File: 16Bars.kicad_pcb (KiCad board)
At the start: 2 copper layers, 28.5 x 105 mm, 40 parts, among them IC1 CD4033BE, IC2 CD4033BE, IC3 CD4510BE, J1 3.5mm_Mono_Switched, J2 Conn_02x05_Odd_Even, Q1 2N3904, Q2 2N3904, Q3 2N3904, Q4 2N3904, Q5 NPN BJT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

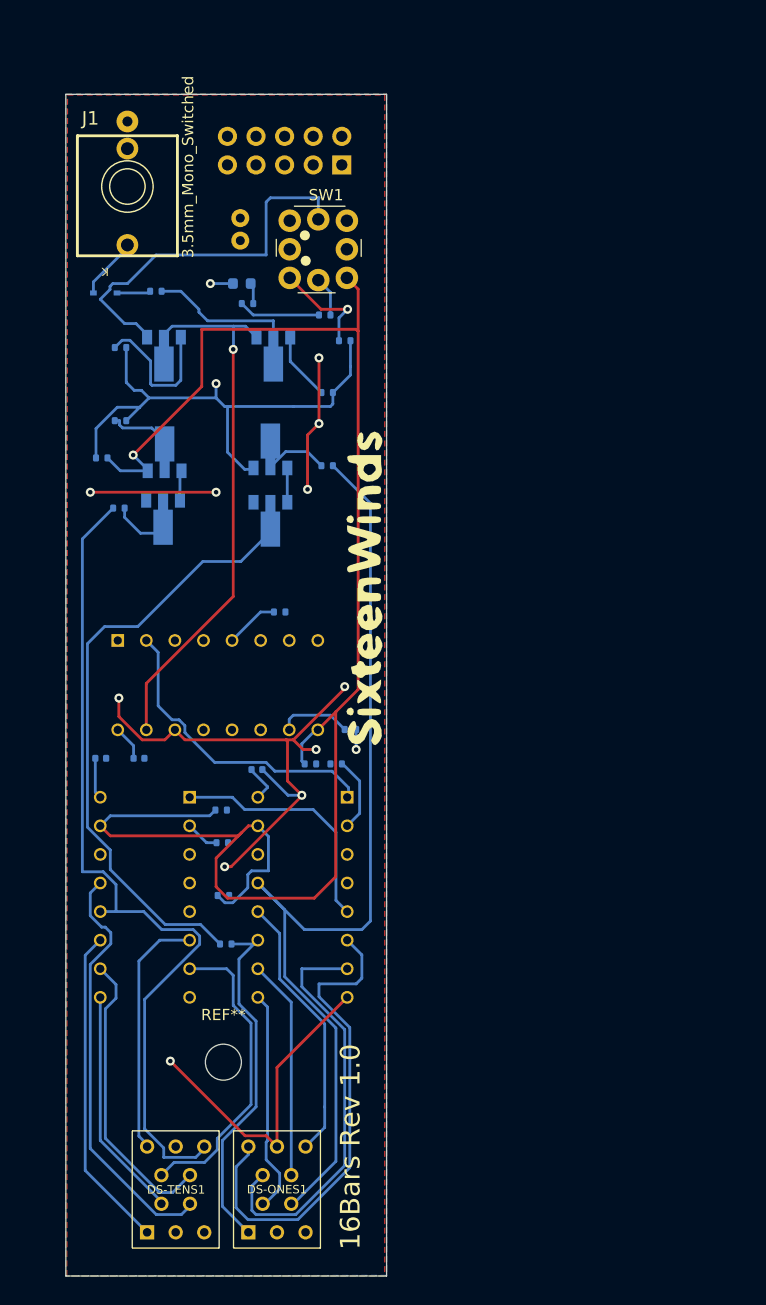
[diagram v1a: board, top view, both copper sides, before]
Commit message: Update PCB with V2 changes
F.Cu SMD assembly will provide much more room for tracks instead of routing around ICs on B.Cu.
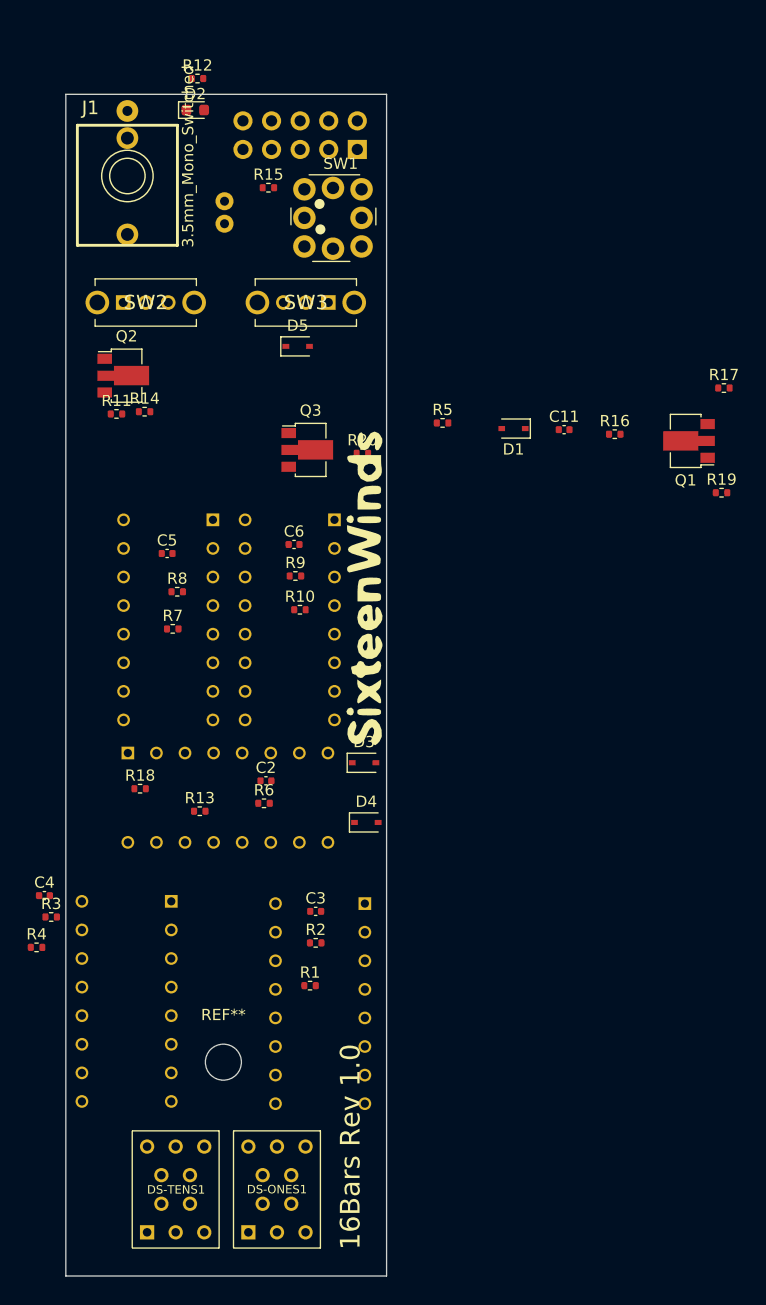
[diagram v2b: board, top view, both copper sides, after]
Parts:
- removed Q4, Q6: 2N3904, Package_TO_SOT_SMD:SOT-89-3
- removed Q5: NPN BJT, Package_TO_SOT_SMD:SOT-89-3
- added C11: 330pf, Capacitor_SMD:C_0402_1005Metric, F.Cu at (100.8, 64.8)
- added C5: 100nf, Capacitor_SMD:C_0402_1005Metric, F.Cu at (65.5, 75.8)
- added C6: 100nf, Capacitor_SMD:C_0402_1005Metric, F.Cu at (76.8, 75.0)
- added D3: 1N5819WS, Diode_SMD:D_SOD-323, F.Cu at (83.0, 94.4)
- added D4: 1N5819WS, Diode_SMD:D_SOD-323, F.Cu at (83.2, 99.7)
- added D5: 1N5819WS, Diode_SMD:D_SOD-323, F.Cu at (77.1, 57.4)
- added IC4: CD4510BE, SamacSys_Parts:DIP794W53P254L1930H508Q16N, B.Cu at (65.6, 81.7)
- added IC5: CD4510BE, SamacSys_Parts:DIP794W53P254L1930H508Q16N, B.Cu at (76.4, 81.7)
- added R19: 10K, Resistor_SMD:R_0402_1005Metric, F.Cu at (114.8, 70.4)
- added R20: 10K, Resistor_SMD:R_0402_1005Metric, F.Cu at (82.9, 66.9)
- added SW2: SW_SPDT - EG1249, EG1249:EG1249, F.Cu at (61.6, 53.5)
- added SW3: SW_SPDT-EG1249, EG1249:EG1249, F.Cu at (79.8, 53.5)
- C2, C3, C4, D2, Q1, Q2, Q3, R1, R10, R11, R12, R13, R14, R15, R16, R17, R18, R2, R3, R4, R6, R7, R8, R9: moved to F.Cu
- D1: value 1N4148 -> 1N5819WS; moved to F.Cu
- R5: value 47K -> 470; moved to F.Cu
- moved R17 55.6 mm to (115.0, 61.1), turned to 0 degrees
- moved R11 48.1 mm to (61.0, 63.4), turned to 0 degrees
- moved D1 38.2 mm to (96.3, 64.7)
- moved Q1 37.7 mm to (111.9, 65.8), turned to 180 degrees
- moved R13 35.4 mm to (68.4, 98.7), turned to 0 degrees
- moved R5 28.0 mm to (90.0, 64.2), turned to 0 degrees
- moved R7 25.4 mm to (66.0, 82.5), turned to 0 degrees
- moved R16 25.4 mm to (105.3, 65.2), turned to 0 degrees
- moved C3 23.4 mm to (78.7, 107.6), turned to 0 degrees
- moved R8 22.2 mm to (66.4, 79.2), turned to 0 degrees
- moved C4 22.0 mm to (54.6, 106.2), turned to 0 degrees
- moved R12 20.5 mm to (68.2, 33.6)
- moved R4 20.4 mm to (53.9, 110.8), turned to 0 degrees
- moved R1 19.8 mm to (78.2, 114.2), turned to 0 degrees
- moved R18 19.4 mm to (63.1, 96.7), turned to 0 degrees
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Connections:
- C2 pad 1: +12V -> GND
- C2 pad 2: GND -> +12V
- D1 pad 1: Net-(D1-Pad1) -> Net-(C11-Pad1)
- D1 pad 2: Net-(D1-Pad2) -> Net-(R5-Pad1)
- IC1 pad 15: /16_BARS_RESET -> /RESET
- IC2 pad 14: unconnected-(IC2-Pad14) -> GND
- IC2 pad 15: /16_BARS_RESET -> /RESET
- IC3 pad 1: GND -> Net-(IC3-Pad1)
- IC3 pad 11: GND -> unconnected-(IC3-Pad11)
- IC3 pad 14: GND -> /4Beats/Bar
- IC3 pad 2: CLOCK_BAR -> /8Beats/Bar
- IC3 pad 5: Net-(IC3-Pad5) -> GND
- IC3 pad 6: GND -> unconnected-(IC3-Pad6)
- IC3 pad 7: unconnected-(IC3-Pad7) -> GND
- IC3 pad 9: /16_BARS_RESET -> Net-(D3-Pad1)
- J1 pad 1: Net-(D1-Pad2) -> Net-(J1-Pad1)
- Q1 pad 1: CLOCK_IN -> GND
- Q2 pad 1: Net-(Q2-Pad1) -> GND
- Q2 pad 2: CLOCK_IN -> Net-(Q2-Pad2)
- Q2 pad 3: Net-(Q2-Pad3) -> /RESET
- Q3 pad 1: Net-(Q3-Pad1) -> GND
- Q3 pad 3: +12V -> CLOCK_IN
- R10 pad 1: /C1 -> Net-(IC5-Pad10)
- R10 pad 2: Net-(Q3-Pad2) -> +12V
- R11 pad 1: /E1 -> Net-(Q2-Pad2)
- R11 pad 2: Net-(Q4-Pad2) -> +12V
- R13 pad 1: +12V -> GND
- R13 pad 2: Net-(Q5-Pad2) -> Net-(IC3-Pad1)
- R14 pad 1: /B2 -> /RESET
- R14 pad 2: Net-(Q6-Pad2) -> +12V
- R16 pad 1: +12V -> Net-(Q1-Pad2)
- R16 pad 2: Net-(R16-Pad2) -> Net-(C11-Pad1)
- R17 pad 1: /16_BARS_RESET -> Net-(Q1-Pad3)
- R2 pad 2: /16_BARS_RESET -> /RESET
- R4 pad 2: /16_BARS_RESET -> /RESET
- R5 pad 1: Net-(Q1-Pad2) -> Net-(R5-Pad1)
- R5 pad 2: Net-(D1-Pad1) -> Net-(J1-Pad1)
- R6 pad 2: /16_BARS_RESET -> Net-(D3-Pad1)
- R7 pad 1: +12V -> /RESET
- R7 pad 2: Net-(Q2-Pad3) -> GND
- R8 pad 1: +12V -> Net-(IC4-Pad10)
- R8 pad 2: Net-(Q1-Pad3) -> +12V
- R9 pad 1: Net-(IC3-Pad5) -> /RESET
- SW1 pad 1: unconnected-(SW1-Pad1) -> GND
- SW1 pad 2: Net-(R16-Pad2) -> GND
- SW1 pad 3: unconnected-(SW1-Pad3) -> Net-(Q2-Pad2)
- SW1 pad 4: /16_BARS_RESET -> Net-(Q2-Pad2)
- SW1 pad L1: Net-(Q2-Pad1) -> CLOCK_IN
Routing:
- net /16_BARS_RESET: track 148.4 -> 0.00 mm, vias 1 -> 0
- net GND: track 106.3 -> 0.00 mm, vias 11 -> 0
- net /C1: track 86.8 -> 0.00 mm
- net /B2: track 75.6 -> 0.00 mm
- net +12V: track 61.4 -> 0.00 mm, vias 3 -> 0
- net Net-(Q4-Pad2): track 57.1 -> 0.00 mm
- net CLOCK_IN: track 48.3 -> 0.00 mm, vias 1 -> 0
- net /F1: track 43.7 -> 0.00 mm
- net /C2: track 37.6 -> 0.00 mm
- net /G1: track 36.8 -> 0.00 mm
- net Net-(Q2-Pad1): track 33.7 -> 0.00 mm
- net /E1: track 32.0 -> 0.00 mm
- net /E2: track 28.8 -> 0.00 mm
- net CLOCK_BAR: track 27.4 -> 0.00 mm
- net /G2: track 27.4 -> 0.00 mm
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- removed copper zone on F.Cu, net +12V
- removed copper zone on B.Cu, net GND

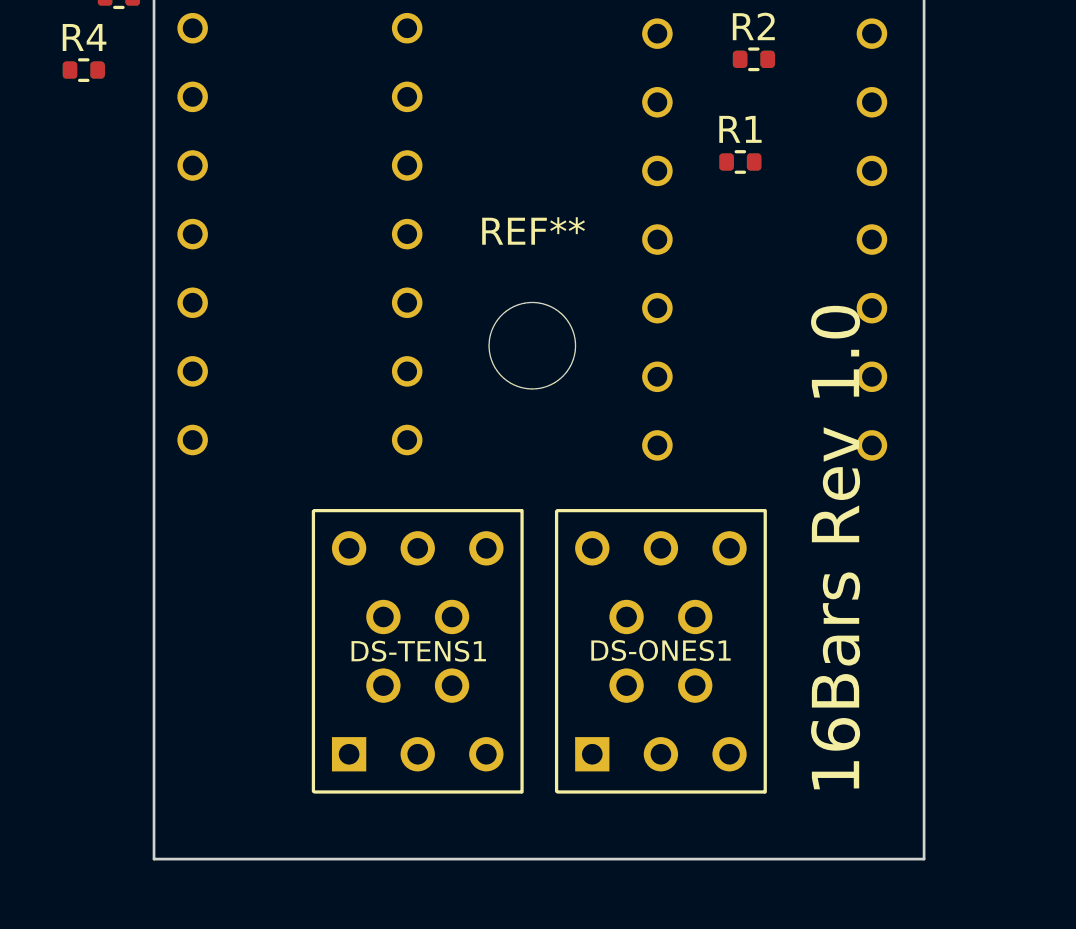
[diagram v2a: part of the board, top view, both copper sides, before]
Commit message: Seven Segment PCB Layout
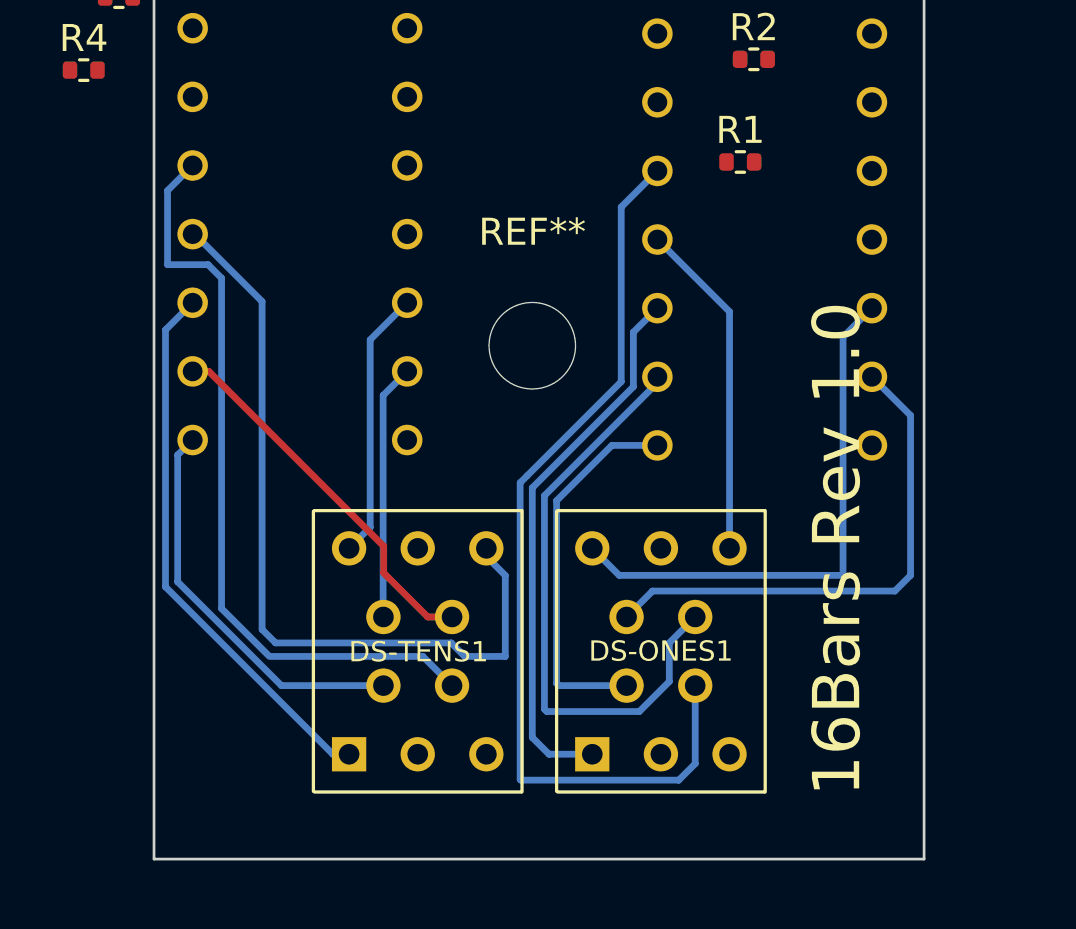
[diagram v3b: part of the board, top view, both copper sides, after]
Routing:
- net /C1: track 0.00 -> 34.3 mm
- net /B2: track 0.00 -> 29.4 mm
- net /C2: track 0.00 -> 28.1 mm
- net /A1: track 0.00 -> 21.9 mm
- net /E2: track 0.00 -> 20.3 mm
- net /E1: track 0.00 -> 20.3 mm
- net /F1: track 0.00 -> 20.0 mm
- net /G1: track 0.00 -> 19.1 mm
- net /D2: track 0.00 -> 14.7 mm
- net /D1: track 0.00 -> 14.0 mm
- net /A2: track 0.00 -> 13.9 mm
- net /B1: track 0.00 -> 12.5 mm
- net /F2: track 0.00 -> 9.98 mm
- net /G2: track 0.00 -> 9.46 mm
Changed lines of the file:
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@@
   )
   (target plus (at 56.5 35) (size 5) (width 0.1) (layer "Edge.Cuts"))
+  (segment (start 70.5 135.5) (end 70.5 126.258938) (width 0.25) (layer "B.Cu") (net 1))
+  (segment (start 74.240489 120.499511) (end 75.13 119.61) (width 0.25) (layer "B.Cu") (net 1))
+  (segment (start 74.240489 122.518449) (end 74.240489 120.499511) (width 0.25) (layer "B.Cu") (net 1))
+  (segment (start 72.72 136.12) (end 71.12 136.12) (width 0.25) (layer "B.Cu") (net 1))
+  (segment (start 70.5 126.258938) (end 74.240489 122.518449) (width 0.25) (layer "B.Cu") (net 1))
+  (segment (start 71.12 136.12) (end 70.5 135.5) (width 0.25) (layer "B.Cu") (net 1))
+  (segment (start 73.445718 124.69) (end 75.13 124.69) (width 0.25) (layer "B.Cu") (net 2))
+  (segment (start 73.99 133.58) (end 71.47904 133.58) (width 0.25) (layer "B.Cu") (net 2))
+  (segment (start 71.39904 126.736678) (end 73.445718 124.69) (width 0.25) (layer "B.Cu") (net 2))
+  (segment (start 71.47904 133.58) (end 71.39904 133.5) (width 0.25) (layer "B.Cu") (net 2))
+  (segment (start 71.39904 133.5) (end 71.39904 126.736678) (width 0.25) (layer "B.Cu") (net 2))
+  (segment (start 73.790969 115.869031) (end 75.13 114.53) (width 0.25) (layer "B.Cu") (net 3))
+  (segment (start 73.790969 122.332252) (end 73.790969 115.869031) (width 0.25) (layer "B.Cu") (net 3))
+  (segment (start 75.920489 137.079511) (end 70.079511 137.079511) (width 0.25) (layer "B.Cu") (net 3))
+  (segment (start 70.05048 137.05048) (end 70.05048 126.07274) (width 0.25) (layer "B.Cu") (net 3))
+  (segment (start 70.05048 126.07274) (end 70.313803 125.809418) (width 0.25) (layer "B.Cu") (net 3))
+  (segment (start 70.313803 125.809418) (end 73.790969 122.332252) (width 0.25) (layer "B.Cu") (net 3))
+  (segment (start 76.53 136.47) (end 75.920489 137.079511) (width 0.25) (layer "B.Cu") (net 3))
+  (segment (start 76.53 133.58) (end 76.53 136.47) (width 0.25) (layer "B.Cu") (net 3))
+  (segment (start 70.079511 137.079511) (end 70.05048 137.05048) (width 0.25) (layer "B.Cu") (net 3))
+  (segment (start 77.8 119.74) (end 75.13 117.07) (width 0.25) (layer "B.Cu") (net 4))
+  (segment (start 77.8 128.5) (end 77.8 119.74) (width 0.25) (layer "B.Cu") (net 4))
+  (segment (start 74.460489 134.539511) (end 71.039511 134.539511) (width 0.25) (layer "B.Cu") (net 5))
+  (segment (start 76.53 131.04) (end 75.570489 131.999511) (width 0.25) (layer "B.Cu") (net 5))
+  (segment (start 75.570489 133.429511) (end 74.460489 134.539511) (width 0.25) (layer "B.Cu") (net 5))
+  (segment (start 70.94952 134.44952) (end 70.94952 126.55048) (width 0.25) (layer "B.Cu") (net 5))
+  (segment (start 75.570489 131.999511) (end 75.570489 133.429511) (width 0.25) (layer "B.Cu") (net 5))
+  (segment (start 70.94952 126.55048) (end 75.13 122.37) (width 0.25) (layer "B.Cu") (net 5))
+  (segment (start 75.13 122.37) (end 75.13 122.15) (width 0.25) (layer "B.Cu") (net 5))
+  (segment (start 71.039511 134.539511) (end 70.94952 134.44952) (width 0.25) (layer "B.Cu") (net 5))
+  (segment (start 84.5 123.58) (end 83.07 122.15) (width 0.25) (layer "B.Cu") (net 7))
+  (segment (start 84.5 129.5) (end 84.5 123.58) (width 0.25) (layer "B.Cu") (net 7))
+  (segment (start 74.949511 130.080489) (end 83.919511 130.080489) (width 0.25) (layer "B.Cu") (net 7))
+  (segment (start 73.99 131.04) (end 74.949511 130.080489) (width 0.25) (layer "B.Cu") (net 7))
+  (segment (start 83.919511 130.080489) (end 84.5 129.5) (width 0.25) (layer "B.Cu") (net 7))
+  (segment (start 82 129.5) (end 82 120.68) (width 0.25) (layer "B.Cu") (net 8))
+  (segment (start 73.72 129.5) (end 82 129.5) (width 0.25) (layer "B.Cu") (net 8))
+  (segment (start 72.72 128.5) (end 73.72 129.5) (width 0.25) (layer "B.Cu") (net 8))
+  (segment (start 82 120.68) (end 83.07 119.61) (width 0.25) (layer "B.Cu") (net 8))
+  (segment (start 63.72 136.12) (end 63.12 136.12) (width 0.25) (layer "B.Cu") (net 9))
+  (segment (start 56.92452 129.92452) (end 56.92452 120.41548) (width 0.25) (layer "B.Cu") (net 9))
+  (segment (start 56.92452 120.41548) (end 57.93 119.41) (width 0.25) (layer "B.Cu") (net 9))
+  (segment (start 63.12 136.12) (end 56.92452 129.92452) (width 0.25) (layer "B.Cu") (net 9))
+  (segment (start 57.37404 125.04596) (end 57.93 124.49) (width 0.25) (layer "B.Cu") (net 10))
+  (segment (start 61.215718 133.58) (end 57.37404 129.738322) (width 0.25) (layer "B.Cu") (net 10))
+  (segment (start 57.37404 129.738322) (end 57.37404 125.04596) (width 0.25) (layer "B.Cu") (net 10))
+  (segment (start 64.99 133.58) (end 61.215718 133.58) (width 0.25) (layer "B.Cu") (net 10))
+  (segment (start 67.53 133.58) (end 66.45 132.5) (width 0.25) (layer "B.Cu") (net 11))
+  (segment (start 57 115.26) (end 57 118) (width 0.25) (layer "B.Cu") (net 11))
+  (segment (start 66.45 132.5) (end 60.864282 132.5) (width 0.25) (layer "B.Cu") (net 11))
+  (segment (start 57 118) (end 58.5 118) (width 0.25) (layer "B.Cu") (net 11))
+  (segment (start 59 130.728564) (end 60.771436 132.5) (width 0.25) (layer "B.Cu") (net 11))
+  (segment (start 57.93 114.33) (end 57 115.26) (width 0.25) (layer "B.Cu") (net 11))
+  (segment (start 58.5 118) (end 59 118.5) (width 0.25) (layer "B.Cu") (net 11))
+  (segment (start 59 118.5) (end 59 130.728564) (width 0.25) (layer "B.Cu") (net 11))
+  (segment (start 69.5 129.5) (end 69.5 132.5) (width 0.25) (layer "B.Cu") (net 12))
+  (segment (start 61 132) (end 60.5 131.5) (width 0.25) (layer "B.Cu") (net 12))
+  (segment (start 60.5 119.364283) (end 58.005717 116.87) (width 0.25) (layer "B.Cu") (net 12))
+  (segment (start 68.8 128.5) (end 68.8 128.8) (width 0.25) (layer "B.Cu") (net 12))
+  (segment (start 68 132.5) (end 67.5 132) (width 0.25) (layer "B.Cu") (net 12))
+  (segment (start 58.005717 116.87) (end 57.93 116.87) (width 0.25) (layer "B.Cu") (net 12))
+  (segment (start 68.8 128.8) (end 69.5 129.5) (width 0.25) (layer "B.Cu") (net 12))
+  (segment (start 67.5 132) (end 61 132) (width 0.25) (layer "B.Cu") (net 12))
+  (segment (start 60.5 131.5) (end 60.5 119.364283) (width 0.25) (layer "B.Cu") (net 12))
+  (segment (start 69.5 132.5) (end 68 132.5) (width 0.25) (layer "B.Cu") (net 12))
+  (segment (start 67.53 131.04) (end 66.631975 131.04) (width 0.25) (layer "F.Cu") (net 13))
+  (segment (start 65 128.423045) (end 58.526955 121.95) (width 0.25) (layer "F.Cu") (net 13))
+  (segment (start 58.526955 121.95) (end 57.93 121.95) (width 0.25) (layer "F.Cu") (net 13))
+  (segment (start 65 129.408025) (end 65 128.423045) (width 0.25) (layer "F.Cu") (net 13))
+  (segment (start 66.631975 131.04) (end 65 129.408025) (width 0.25) (layer "F.Cu") (net 13))
+  (segment (start 64.99 131.04) (end 64.980489 131.030489) (width 0.25) (layer "B.Cu") (net 14))
+  (segment (start 64.980489 122.839511) (end 65.87 121.95) (width 0.25) (layer "B.Cu") (net 14))
+  (segment (start 64.980489 131.030489) (end 64.980489 122.839511) (width 0.25) (layer "B.Cu") (net 14))
+  (segment (start 63.72 128.5) (end 64.5 127.72) (width 0.25) (layer "B.Cu") (net 15))
+  (segment (start 64.5 120.78) (end 65.87 119.41) (width 0.25) (layer "B.Cu") (net 15))
+  (segment (start 64.5 127.72) (end 64.5 120.78) (width 0.25) (layer "B.Cu") (net 15))
 )

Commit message: More PCB Layout
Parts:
- moved R18 14.1 mm to (77.0, 99.0), turned to -90 degrees
- moved C2 12.8 mm to (62.0, 99.5), turned to -90 degrees
- moved D3 11.1 mm to (77.5, 104.0), turned to 180 degrees
- moved R3 8.91 mm to (64.0, 109.5), turned to 180 degrees
- moved R4 7.22 mm to (61.0, 109.5), turned to 180 degrees
- moved R13 7.16 mm to (62.0, 95.5), turned to 90 degrees
- moved C4 6.45 mm to (61.0, 107.0), turned to 180 degrees
- moved R6 5.48 mm to (79.5, 99.0), turned to -90 degrees
- moved R1 5.47 mm to (81.0, 109.5), turned to 180 degrees
- moved D4 4.46 mm to (82.0, 104.0)
- moved R2 1.14 mm to (78.0, 109.5), turned to 180 degrees
- moved C3 0.92 mm to (78.0, 107.0), turned to 180 degrees
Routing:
- net Net-(D3-Pad1): track 0.00 -> 8.13 mm
- net +12V: track 0.00 -> 6.63 mm
- net /RESET: track 0.00 -> 5.04 mm
- net Net-(IC3-Pad10): track 0.00 -> 2.08 mm
- net Net-(IC1-Pad2): track 0.00 -> 1.59 mm
- net Net-(IC3-Pad1): track 0.00 -> 1.46 mm
- net Net-(IC2-Pad2): track 0.00 -> 1.46 mm
